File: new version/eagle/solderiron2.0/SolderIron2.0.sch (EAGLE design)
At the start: 36 parts, among them J1 DCJ0202, X1 22-23-2021, X2 PG203J

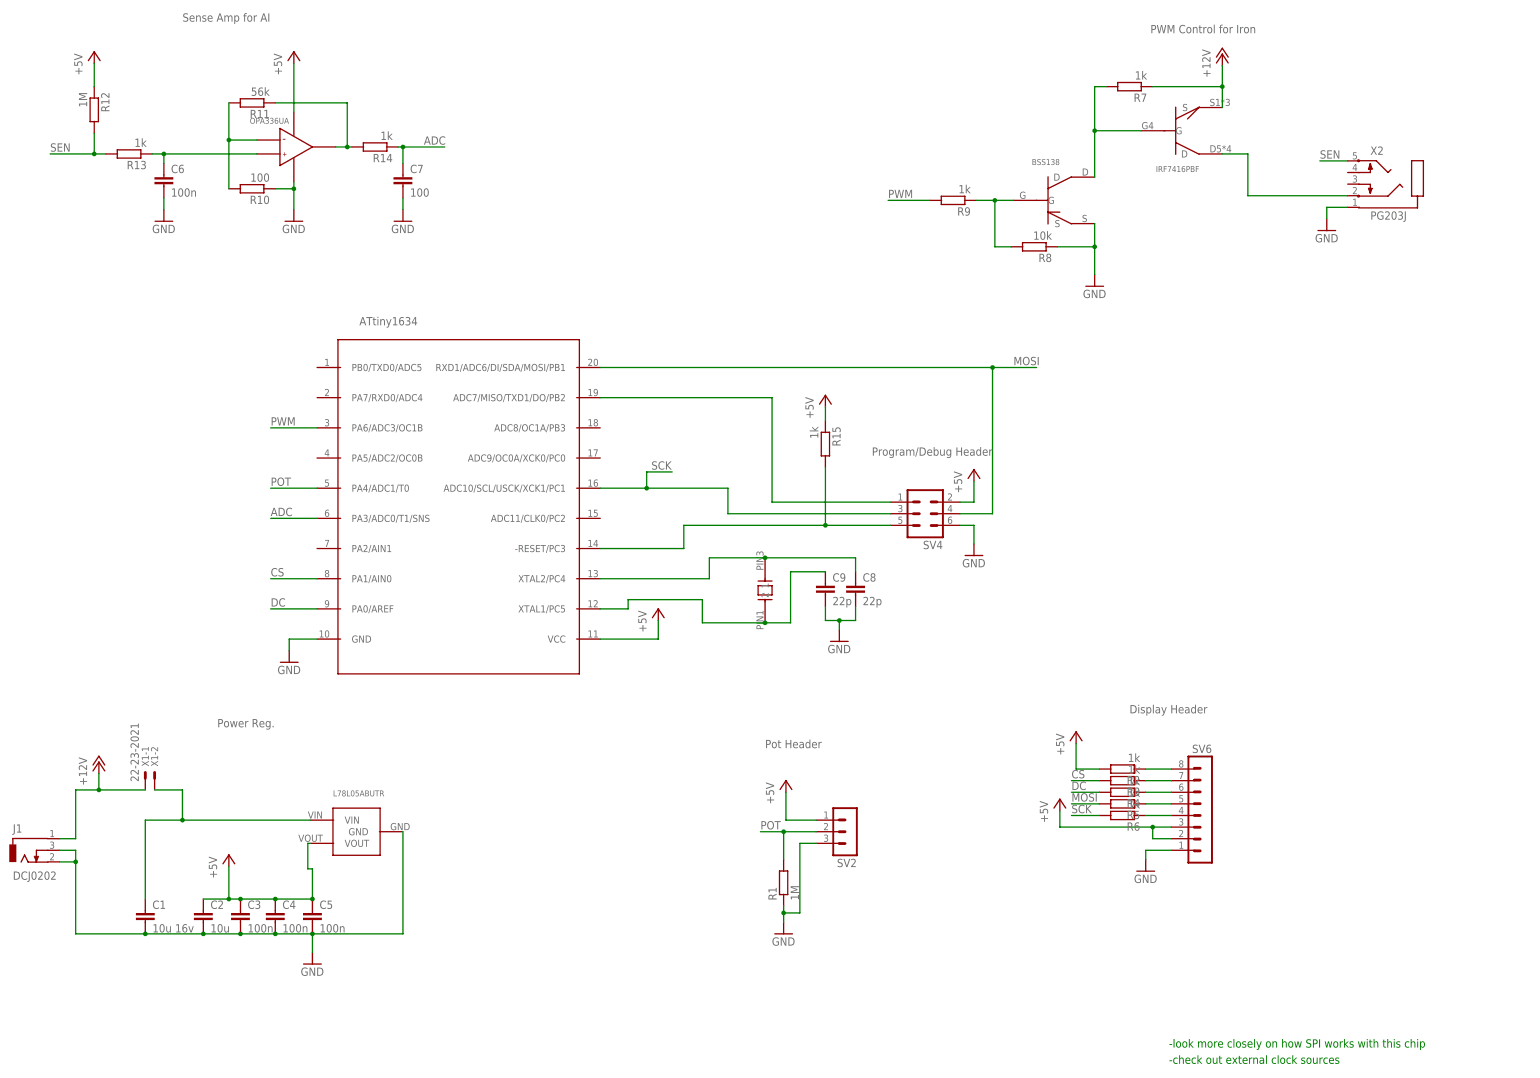
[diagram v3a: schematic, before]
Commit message: finished PCB part layout
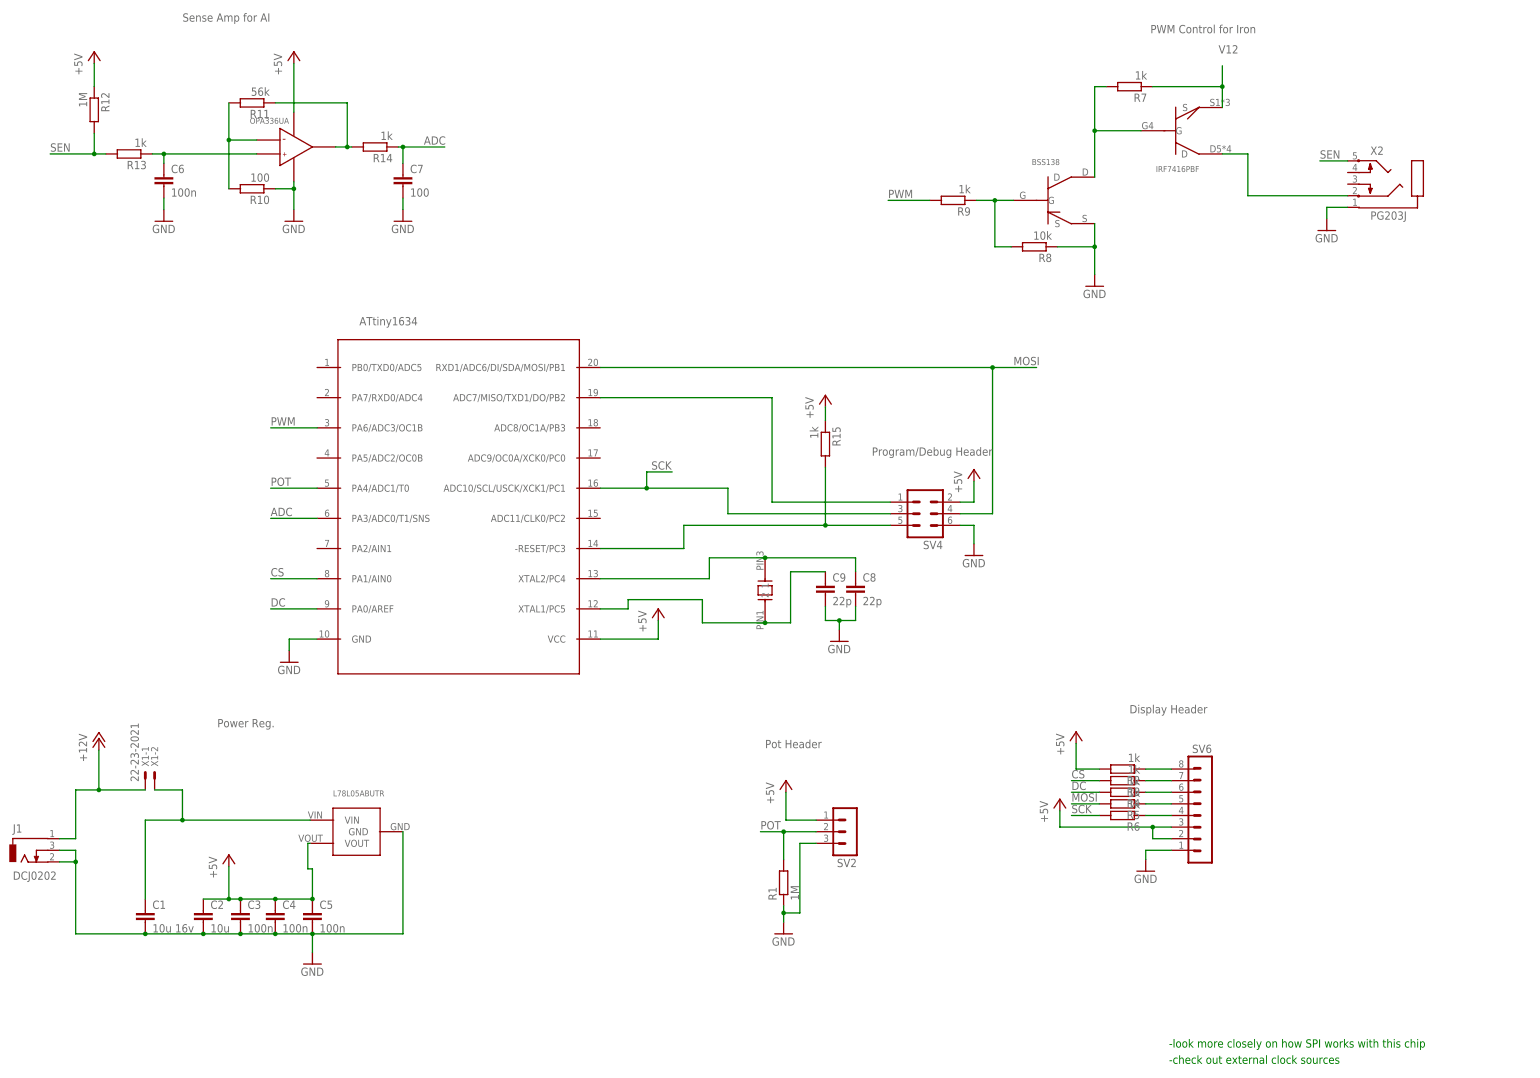
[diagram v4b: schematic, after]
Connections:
- removed net N$3: C1.1, U$2.VIN, X1-2.S
- new net V12: C1.1, R7.1, U$1.S, U$2.VIN, X1-2.S
- net +12V: no longer R7.1, U$1.S
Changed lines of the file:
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@@
 <setting verticaltext="up"/>
 </settings>
-<grid distance="0.5" unitdist="mm" unit="mm" style="lines" multiple="1" display="yes" altdistance="0.01" altunitdist="inch" altunit="inch"/>
+<grid distance="0.1" unitdist="inch" unit="inch" style="lines" multiple="1" display="no" altdistance="0.01" altunitdist="inch" altunit="inch"/>
 <layers>
 <layer number="1" name="Top" color="4" fill="1" visible="no" active="no"/>
@@
 <part name="GND4" library="supply1" deviceset="GND" device=""/>
 <part name="U$1" library="solderstation" deviceset="IRF7416PBF" device=""/>
-<part name="P+1" library="supply1" deviceset="+12V" device=""/>
 <part name="U$3" library="solderstation" deviceset="BSS138" device=""/>
 <part name="R7" library="eagle-ltspice" deviceset="R" device="R0603" value="1k"/>
@@
 <attribute name="NAME" x="-121.738" y="-49.46" size="1.524" layer="95" rot="R90"/>
 </instance>
-<instance part="P+6" gate="1" x="-134.5" y="-48.5"/>
+<instance part="P+6" gate="1" x="-134.5" y="-43.42"/>
 <instance part="X2" gate="1" x="147" y="78.5"/>
 <instance part="GND4" gate="1" x="130" y="66"/>
 <instance part="U$1" gate="G$1" x="100" y="87.5" rot="R180"/>
-<instance part="P+1" gate="1" x="107.5" y="104"/>
 <instance part="U$3" gate="G$1" x="72.5" y="72.5" rot="MR0"/>
 <instance part="R7" gate="G$1" x="87.5" y="97" rot="R180"/>
@@
 </segment>
 </net>
-<net name="N$3" class="0">
+<net name="V12" class="0">
 <segment>
 <wire x1="-89" y1="-61" x2="-116.5" y2="-61" width="0.1524" layer="91"/>
@@
 <junction x="-116.5" y="-61"/>
 </segment>
-</net>
-<net name="+12V" class="0">
-<segment>
-<wire x1="-134.5" y1="-54.5" x2="-139.5" y2="-54.5" width="0.1524" layer="91"/>
-<wire x1="-139.5" y1="-54.5" x2="-139.5" y2="-65" width="0.1524" layer="91"/>
-<pinref part="J1" gate="G$1" pin="1"/>
-<wire x1="-139.5" y1="-65" x2="-143" y2="-65" width="0.1524" layer="91"/>
-<pinref part="P+6" gate="1" pin="+12V"/>
-<wire x1="-134.5" y1="-51" x2="-134.5" y2="-54.5" width="0.1524" layer="91"/>
-<pinref part="X1" gate="-1" pin="S"/>
-<wire x1="-134.5" y1="-54.5" x2="-124.5" y2="-54.5" width="0.1524" layer="91"/>
-<junction x="-134.5" y="-54.5"/>
-</segment>
-<segment>
-<pinref part="P+1" gate="1" pin="+12V"/>
+<segment>
 <pinref part="U$1" gate="G$1" pin="S"/>
 <wire x1="107.5" y1="101.5" x2="107.5" y2="97" width="0.1524" layer="91"/>
@@
 <wire x1="92.5" y1="97" x2="107.5" y2="97" width="0.1524" layer="91"/>
 <junction x="107.5" y="97"/>
+<label x="106.68" y="104.14" size="1.778" layer="95"/>
 </segment>
 </net>
+<net name="+12V" class="0">
+<segment>
+<wire x1="-134.5" y1="-54.5" x2="-139.5" y2="-54.5" width="0.1524" layer="91"/>
+<wire x1="-139.5" y1="-54.5" x2="-139.5" y2="-65" width="0.1524" layer="91"/>
+<pinref part="J1" gate="G$1" pin="1"/>
+<wire x1="-139.5" y1="-65" x2="-143" y2="-65" width="0.1524" layer="91"/>
+<pinref part="P+6" gate="1" pin="+12V"/>
+<wire x1="-134.5" y1="-45.92" x2="-134.5" y2="-54.5" width="0.1524" layer="91"/>
+<pinref part="X1" gate="-1" pin="S"/>
+<wire x1="-134.5" y1="-54.5" x2="-124.5" y2="-54.5" width="0.1524" layer="91"/>
+<junction x="-134.5" y="-54.5"/>
+</segment>
+</net>
